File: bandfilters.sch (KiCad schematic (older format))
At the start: 25 parts, among them K1 BAND3_IN, K2 BAND2_IN, K3 BAND1_IN, K4 BAND3_OUT, K5 BAND2_OUT, K6 BAND1_OUT

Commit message: Connected all mcu VSS and VDD pins.
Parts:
- K1, K2, K3, K4, K5, K6: footprint (none) -> nu9j-footprints:EC2-12NU
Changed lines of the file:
@@
 F 0 "K1" H 4150 2900 70  0000 C CNN
 F 1 "BAND3_IN" H 4350 2000 70  0000 C CNN
-F 2 "" H 4200 2500 60  0000 C CNN
+F 2 "nu9j-footprints:EC2-12NU" H 4200 2500 60  0001 C CNN
 F 3 "" H 4200 2500 60  0000 C CNN
 	1    4200 2500
@@
 F 0 "K2" H 4150 4200 70  0000 C CNN
 F 1 "BAND2_IN" H 4350 3300 70  0000 C CNN
-F 2 "" H 4200 3800 60  0000 C CNN
+F 2 "nu9j-footprints:EC2-12NU" H 4200 3800 60  0001 C CNN
 F 3 "" H 4200 3800 60  0000 C CNN
 	1    4200 3800
@@
 F 0 "K3" H 4150 5500 70  0000 C CNN
 F 1 "BAND1_IN" H 4350 4600 70  0000 C CNN
-F 2 "" H 4200 5100 60  0000 C CNN
+F 2 "nu9j-footprints:EC2-12NU" H 4200 5100 60  0001 C CNN
 F 3 "" H 4200 5100 60  0000 C CNN
 	1    4200 5100
@@
 F 0 "K6" H 7450 5500 70  0000 C CNN
 F 1 "BAND1_OUT" H 7650 4600 70  0000 C CNN
-F 2 "" H 7500 5100 60  0000 C CNN
+F 2 "nu9j-footprints:EC2-12NU" H 7500 5100 60  0001 C CNN
 F 3 "" H 7500 5100 60  0000 C CNN
 	1    7500 5100
@@
 F 0 "K4" H 7450 2900 70  0000 C CNN
 F 1 "BAND3_OUT" H 7650 2000 70  0000 C CNN
-F 2 "" H 7500 2500 60  0000 C CNN
+F 2 "nu9j-footprints:EC2-12NU" H 7500 2500 60  0001 C CNN
 F 3 "" H 7500 2500 60  0000 C CNN
 	1    7500 2500
@@
 F 0 "K5" H 7450 4200 70  0000 C CNN
 F 1 "BAND2_OUT" H 7650 3300 70  0000 C CNN
-F 2 "" H 7500 3800 60  0000 C CNN
+F 2 "nu9j-footprints:EC2-12NU" H 7500 3800 60  0001 C CNN
 F 3 "" H 7500 3800 60  0000 C CNN
 	1    7500 3800

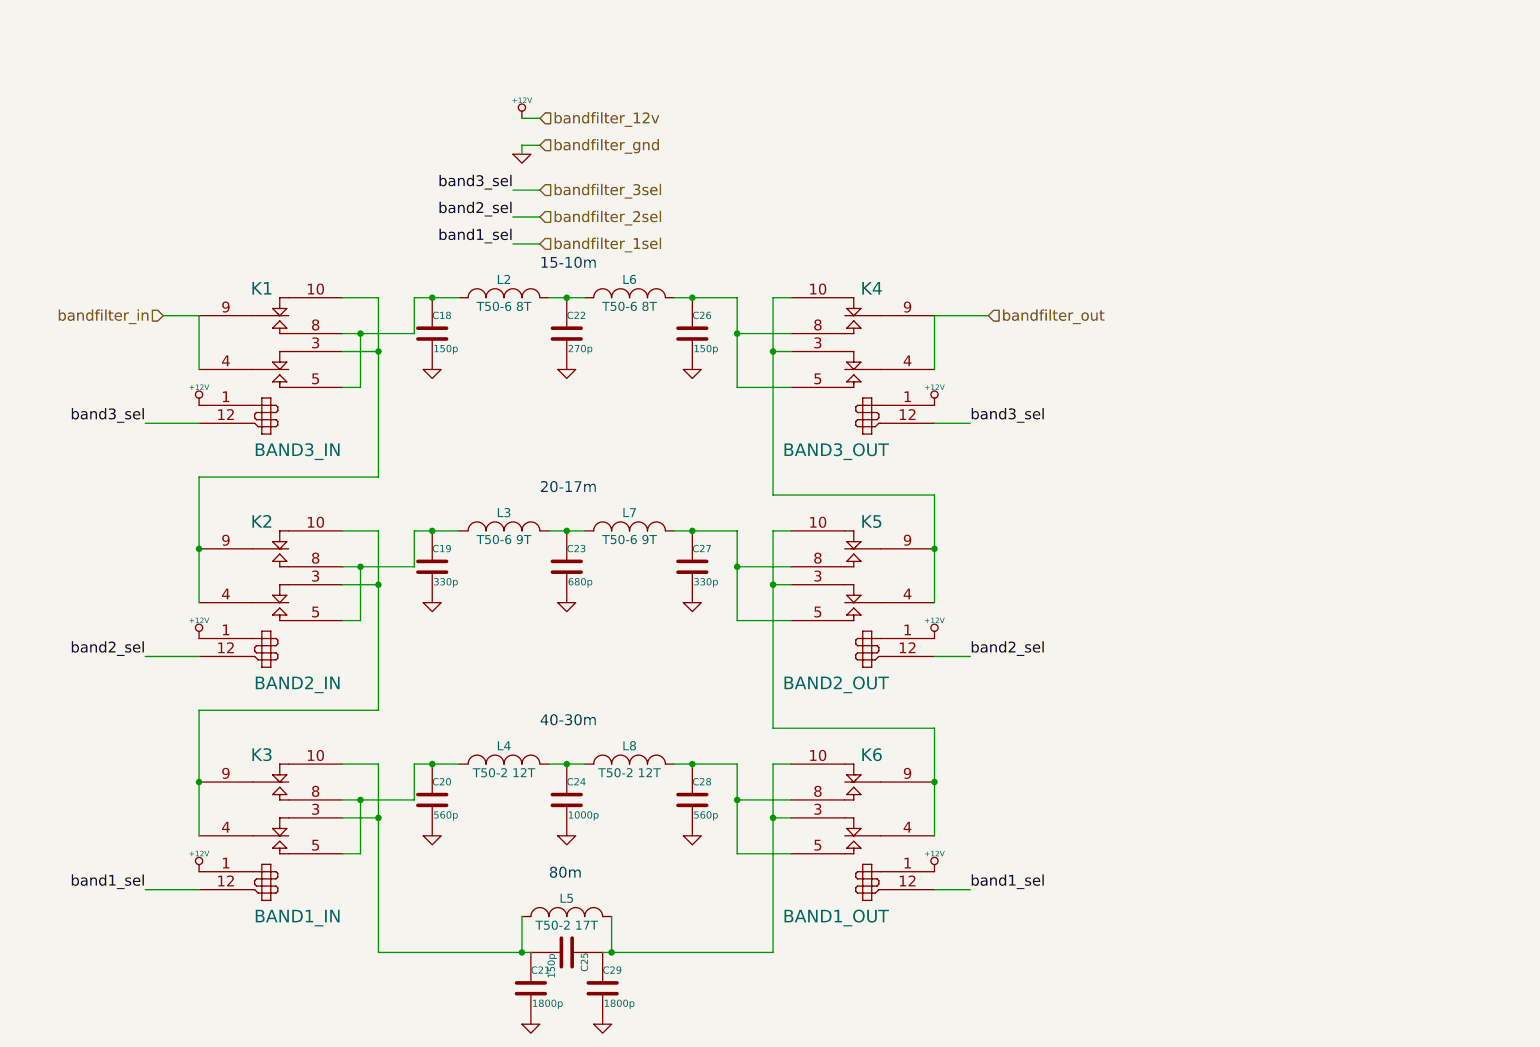
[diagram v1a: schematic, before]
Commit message: Fixed issues found with test board
- Added MOSFETs to relay switch lines from MCU
- Reconnected SWR in/out to actual ADC pins
- Changed LM3940 footprint to SOT223
- Added 4th mounting hole
- Swapped joystick for nav button
- Extended pads of STM32F401 for easier soldering
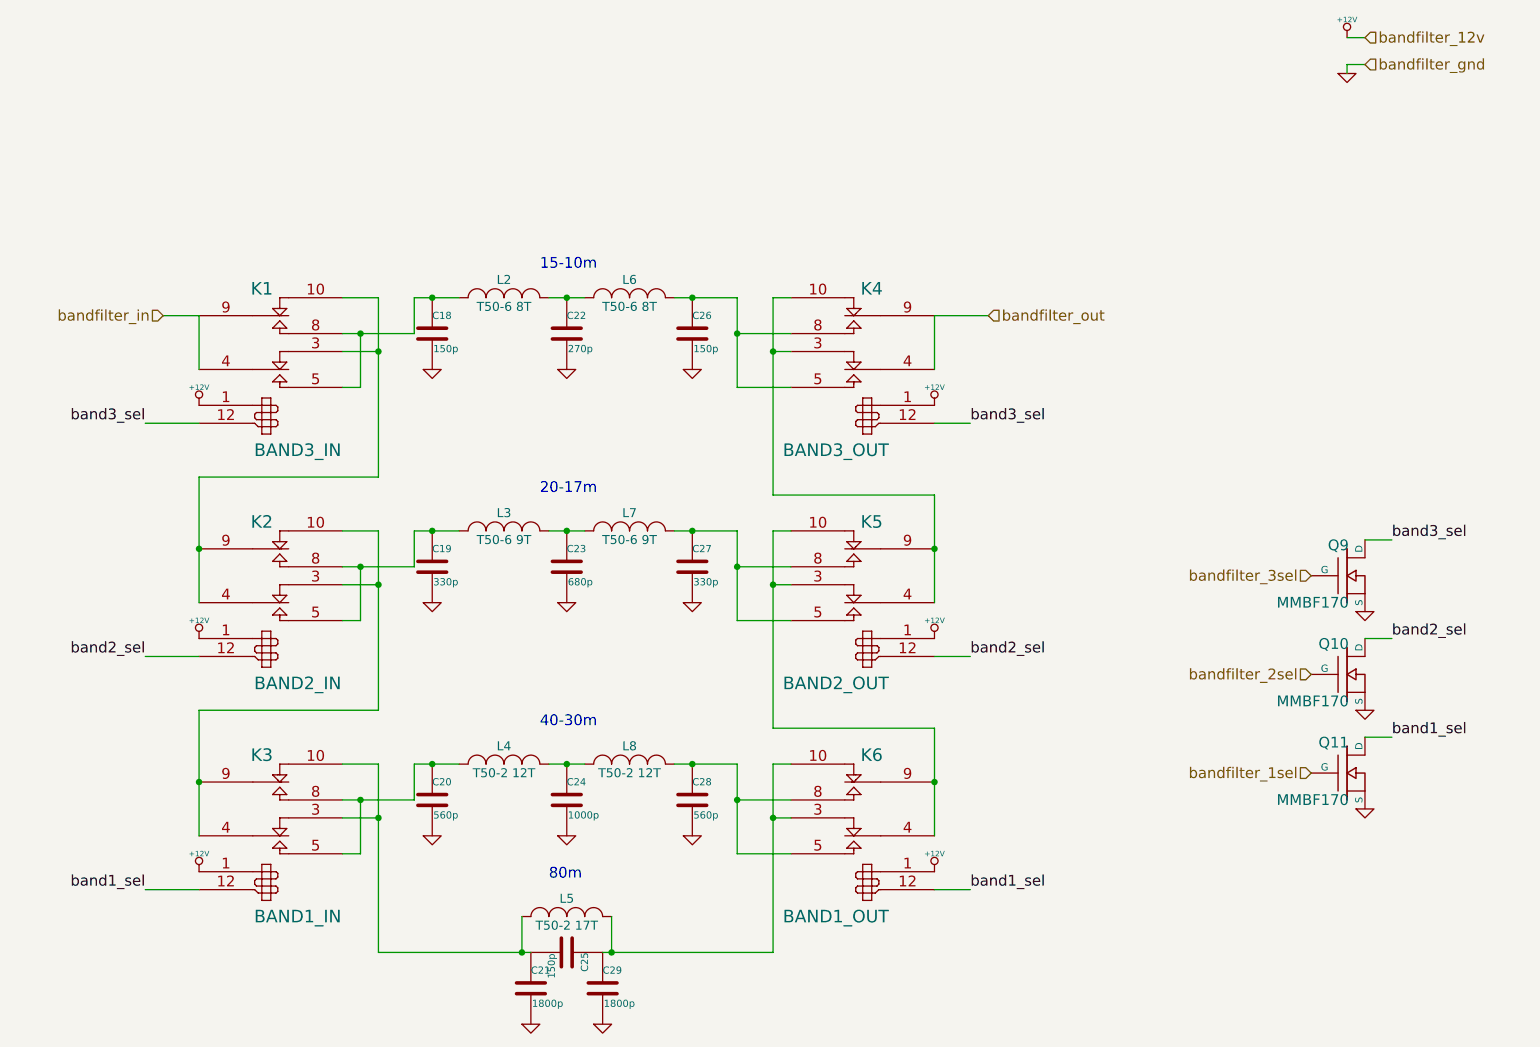
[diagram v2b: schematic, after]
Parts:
- added Q10, Q11, Q9: MMBF170, nu9j-footprints:sot23-DGS, symbol MOSFET_N
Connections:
- net GND: now also Q10.S, Q11.S, Q9.S
- net bandfilter_1sel: now also Q11.G; no longer K3.12, K6.12
- net bandfilter_2sel: now also Q10.G; no longer K2.12, K5.12
- net bandfilter_3sel: now also Q9.G; no longer K1.12, K4.12
- new net band1_sel: K3.12, K6.12, Q11.D
- new net band2_sel: K2.12, K5.12, Q10.D
- new net band3_sel: K1.12, K4.12, Q9.D
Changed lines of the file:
@@
 L +12V #PWR072
 U 1 1 5470E689
-P 5600 1150
-F 0 "#PWR072" H 5600 1100 20  0001 C CNN
-F 1 "+12V" H 5600 1250 30  0000 C CNN
-F 2 "" H 5600 1150 60  0000 C CNN
-F 3 "" H 5600 1150 60  0000 C CNN
-	1    5600 1150
+P 10200 700
+F 0 "#PWR072" H 10200 650 20  0001 C CNN
+F 1 "+12V" H 10200 800 30  0000 C CNN
+F 2 "" H 10200 700 60  0000 C CNN
+F 3 "" H 10200 700 60  0000 C CNN
+	1    10200 700
 	1    0    0    -1
 $EndComp
@@
 L GND #PWR073
 U 1 1 5470E69D
-P 5600 1350
-F 0 "#PWR073" H 5600 1350 30  0001 C CNN
-F 1 "GND" H 5600 1280 30  0001 C CNN
-F 2 "" H 5600 1350 60  0000 C CNN
-F 3 "" H 5600 1350 60  0000 C CNN
-	1    5600 1350
+P 10200 900
+F 0 "#PWR073" H 10200 900 30  0001 C CNN
+F 1 "GND" H 10200 830 30  0001 C CNN
+F 2 "" H 10200 900 60  0000 C CNN
+F 3 "" H 10200 900 60  0000 C CNN
+	1    10200 900
 	1    0    0    -1
 $EndComp
-Wire Wire Line
-	5700 1550 5550 1550
-Wire Wire Line
-	5700 1700 5550 1700
-Wire Wire Line
-	5700 1850 5550 1850
-Text Label 5550 1550 2    60   ~ 0
+Text Label 10450 3500 0    60   ~ 0
 band3_sel
-Text Label 5550 1700 2    60   ~ 0
+Text Label 10450 4050 0    60   ~ 0
 band2_sel
-Text Label 5550 1850 2    60   ~ 0
+Text Label 10450 4600 0    60   ~ 0
 band1_sel
 Wire Wire Line
-	5600 1150 5700 1150
+	10200 700  10300 700
 Wire Wire Line
-	5600 1350 5600 1300
+	10200 900  10200 850
 Wire Wire Line
-	5600 1300 5700 1300
-Text HLabel 5700 1150 2    60   Input ~ 0
+	10200 850  10300 850
+Text HLabel 10300 700  2    60   Input ~ 0
 bandfilter_12v
-Text HLabel 5700 1300 2    60   Input ~ 0
+Text HLabel 10300 850  2    60   Input ~ 0
 bandfilter_gnd
-Text HLabel 5700 1550 2    60   Input ~ 0
+Text HLabel 10000 3700 0    60   Input ~ 0
 bandfilter_3sel
-Text HLabel 5700 1700 2    60   Input ~ 0
+Text HLabel 10000 4250 0    60   Input ~ 0
 bandfilter_2sel
-Text HLabel 5700 1850 2    60   Input ~ 0
+Text HLabel 10000 4800 0    60   Input ~ 0
 bandfilter_1sel
 Wire Wire Line
@@
 	-1   0    0    -1
 $EndComp
+$Comp
+L MOSFET_N Q9
+U 1 1 54C46126
+P 10200 3700
+F 0 "Q9" H 10210 3870 60  0000 R CNN
+F 1 "MMBF170" H 10210 3550 60  0000 R CNN
+F 2 "nu9j-footprints:sot23-DGS" H 10200 3700 60  0001 C CNN
+F 3 "" H 10200 3700 60  0000 C CNN
+	1    10200 3700
+	1    0    0    -1
+$EndComp
+$Comp
+L GND #PWR074
+U 1 1 54C463F8
+P 10300 3900
+F 0 "#PWR074" H 10300 3900 30  0001 C CNN
+F 1 "GND" H 10300 3830 30  0001 C CNN
+F 2 "" H 10300 3900 60  0000 C CNN
+F 3 "" H 10300 3900 60  0000 C CNN
+	1    10300 3900
+	1    0    0    -1
+$EndComp
+$Comp
+L MOSFET_N Q10
+U 1 1 54C4649F
+P 10200 4250
+F 0 "Q10" H 10210 4420 60  0000 R CNN
+F 1 "MMBF170" H 10210 4100 60  0000 R CNN
+F 2 "nu9j-footprints:sot23-DGS" H 10200 4250 60  0001 C CNN
+F 3 "" H 10200 4250 60  0000 C CNN
+	1    10200 4250
+	1    0    0    -1
+$EndComp
+$Comp
+L GND #PWR075
+U 1 1 54C464EC
+P 10300 4450
+F 0 "#PWR075" H 10300 4450 30  0001 C CNN
+F 1 "GND" H 10300 4380 30  0001 C CNN
+F 2 "" H 10300 4450 60  0000 C CNN
+F 3 "" H 10300 4450 60  0000 C CNN
+	1    10300 4450
+	1    0    0    -1
+$EndComp
+$Comp
+L MOSFET_N Q11
+U 1 1 54C46512
+P 10200 4800
+F 0 "Q11" H 10210 4970 60  0000 R CNN
+F 1 "MMBF170" H 10210 4650 60  0000 R CNN
+F 2 "nu9j-footprints:sot23-DGS" H 10200 4800 60  0001 C CNN
+F 3 "" H 10200 4800 60  0000 C CNN
+	1    10200 4800
+	1    0    0    -1
+$EndComp
+$Comp
+L GND #PWR076
+U 1 1 54C46558
+P 10300 5000
+F 0 "#PWR076" H 10300 5000 30  0001 C CNN
+F 1 "GND" H 10300 4930 30  0001 C CNN
+F 2 "" H 10300 5000 60  0000 C CNN
+F 3 "" H 10300 5000 60  0000 C CNN
+	1    10300 5000
+	1    0    0    -1
+$EndComp
+Wire Wire Line
+	10300 3500 10450 3500
+Wire Wire Line
+	10300 4050 10450 4050
+Wire Wire Line
+	10300 4600 10450 4600
 $EndSCHEMATC

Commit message: Schematic changes to go with #3 (extending sot23 pads)
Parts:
- Q10, Q11, Q9: footprint nu9j-footprints:sot23-DGS -> nu9j-footprints:SOT-23-DGS_HandSoldering
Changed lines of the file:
@@
 F 0 "Q9" H 10210 3870 60  0000 R CNN
 F 1 "MMBF170" H 10210 3550 60  0000 R CNN
-F 2 "nu9j-footprints:sot23-DGS" H 10200 3700 60  0001 C CNN
+F 2 "nu9j-footprints:SOT-23-DGS_HandSoldering" H 10200 3700 60  0001 C CNN
 F 3 "" H 10200 3700 60  0000 C CNN
 	1    10200 3700
@@
 F 0 "Q10" H 10210 4420 60  0000 R CNN
 F 1 "MMBF170" H 10210 4100 60  0000 R CNN
-F 2 "nu9j-footprints:sot23-DGS" H 10200 4250 60  0001 C CNN
+F 2 "nu9j-footprints:SOT-23-DGS_HandSoldering" H 10200 4250 60  0001 C CNN
 F 3 "" H 10200 4250 60  0000 C CNN
 	1    10200 4250
@@
 F 0 "Q11" H 10210 4970 60  0000 R CNN
 F 1 "MMBF170" H 10210 4650 60  0000 R CNN
-F 2 "nu9j-footprints:sot23-DGS" H 10200 4800 60  0001 C CNN
+F 2 "nu9j-footprints:SOT-23-DGS_HandSoldering" H 10200 4800 60  0001 C CNN
 F 3 "" H 10200 4800 60  0000 C CNN
 	1    10200 4800
